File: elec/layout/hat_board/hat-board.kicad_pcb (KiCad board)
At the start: 4 copper layers, 108 x 115.9 mm, 82 parts, among them P1 HatButtonAntenna, U1 _NXP_Semicon_PN5321A3HN_C106_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, U10 _OPSCO_Optoelectronics_SK6805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, U11 _OPSCO_Optoelectronics_SK6805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, U12 _OPSCO_Optoelectronics_SK6805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, U13 _OPSCO_Optoelectronics_SK6805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, U14 _OPSCO_Optoelectronics_SK6805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, U15 _OPSCO_Optoelectronics_SK6805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, U16 _OPSCO_Optoelectronics_SK6805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, U17 _OPSCO_Optoelectronics_SK6805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, U18 _OPSCO_Optoelectronics_SK6805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, U19 _OPSCO_Optoelectronics_SK6805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, U2 _OPSCO_Optoelectronics_SK6805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, U20 _OPSCO_Optoelectronics_SK6805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, U21 _OPSCO_Optoelectronics_SK6805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, U22 _OPSCO_Optoelectronics_SK6805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, U23 _OPSCO_Optoelectronics_SK6805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, U24 _OPSCO_Optoelectronics_SK6805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, U25 _Microchip_Tech_CAP1188_1_CP_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, U3 _OPSCO_Optoelectronics_SK6805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, U4 _OPSCO_Optoelectronics_SK6805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, U5 _OPSCO_Optoelectronics_SK6805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, U6 _OPSCO_Optoelectronics_SK6805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, U7 _OPSCO_Optoelectronics_SK6805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, U8 _OPSCO_Optoelectronics_SK6805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, U9 _OPSCO_Optoelectronics_SK6805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

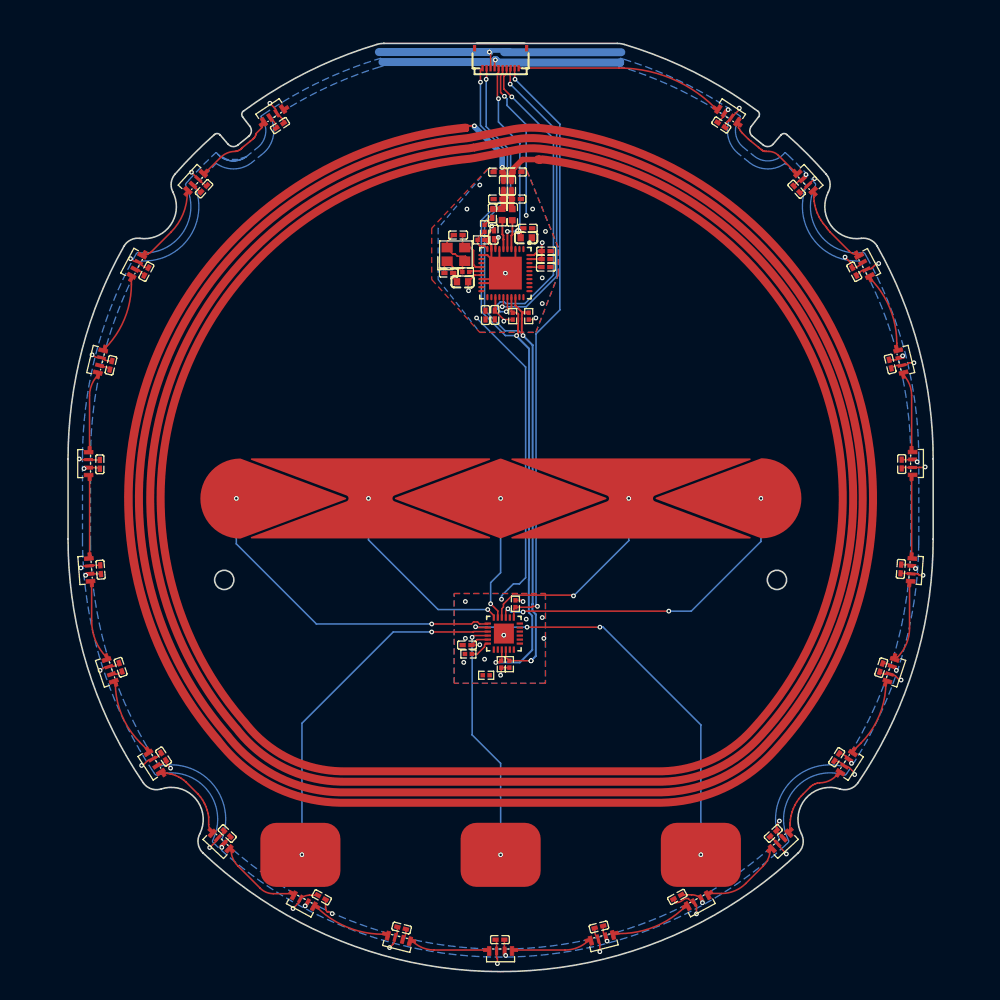
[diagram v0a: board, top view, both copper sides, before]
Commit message: Fix: hat layout
Depends on #23
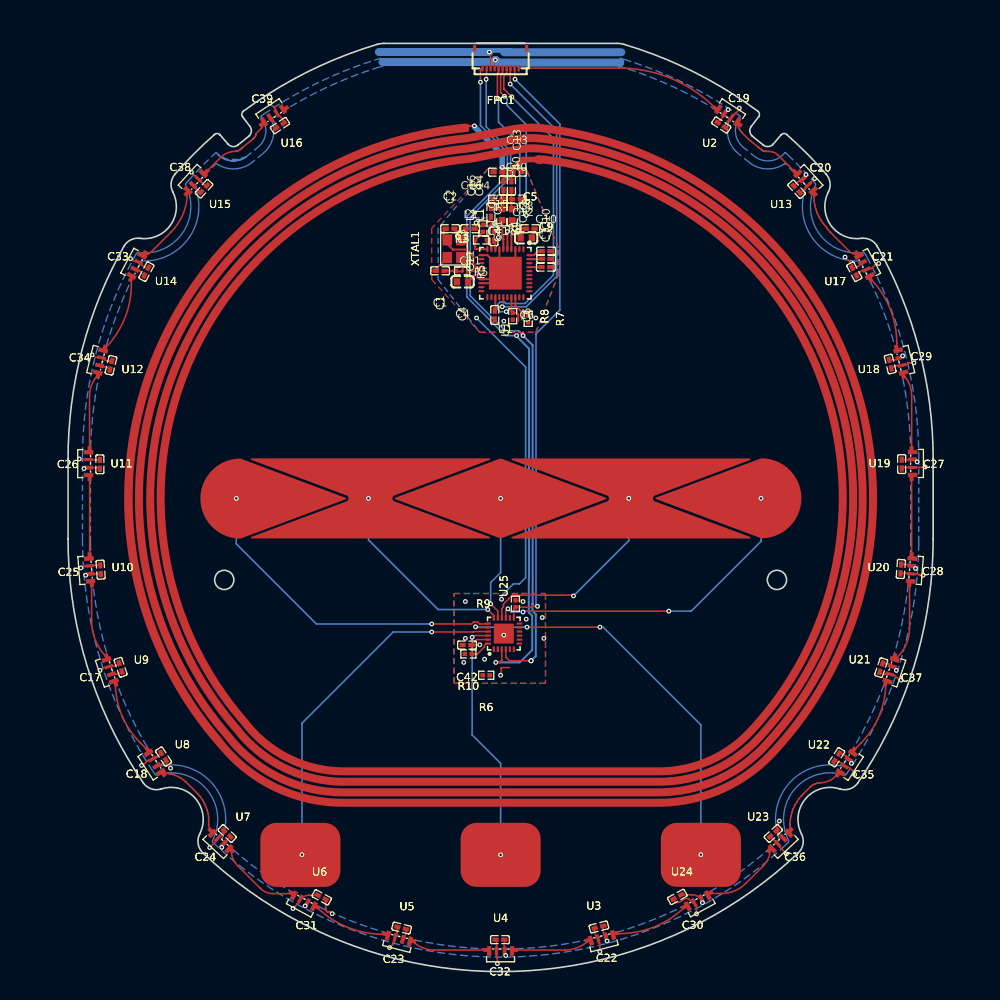
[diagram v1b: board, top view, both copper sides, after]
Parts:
- removed R1, R2: 5.1kΩ ±1% 62.5mW, lcsc:R0402
- C1, C10, C11, C12, C13, C14, C15, C16, C17, C18, C19, C2, C20, C21, C22, C23, C24, C25, C26, C27, C28, C29, C3, C30, C31, C32, C33, C34, C35, C36, C37, C38, C39, C40, C41, C42, C5, C6, C7, C9: footprint lcsc:C0402 -> atopile:C0402-b3ef17
- C4, C8: footprint lcsc:C0603 -> atopile:C0603-bd72f6
- FPC1: value TE_Connectivity_1_2328702_0 -> (none); footprint lcsc:FPC-SMD_10P-P0.50_HDGC_0.5K-HX-10PWB -> atopile:FPC-SMD_10P-P0.50_HDGC_0.5K-HX-10PWB-40cf1c
- L1, L2: value 560nH ±5% 450mA 480mΩ -> (none); footprint lcsc:IND-SMD_L1.6-W0.8-1 -> atopile:IND-SMD_L1.6-W0.8-1-cea827
- P1: value HatButtonAntenna -> (none)
- R10, R3, R4, R5, R6, R9: footprint lcsc:R0402 -> atopile:R0402-56259e
- R7, R8: value 5.1kΩ ±1% 62.5mW -> 100kΩ ±1% 62.5mW; footprint lcsc:R0402 -> atopile:R0402-56259e
- U1: value _NXP_Semicon_PN5321A3HN_C106_51 -> (none); footprint lcsc:QFN-40_L6.0-W6.0-P0.50-BL-EP4.1 -> atopile:QFN-40_L6.0-W6.0-P0.50-BL-EP4.1-54a13c
- U10, U11, U12, U13, U14, U15, U16, U17, U18, U19, U2, U20, U21, U22, U23, U24, U3, U4, U5, U6, U7, U8, U9: value _OPSCO_Optoelectronics_SK6805SIDE_G_001 -> (none); footprint lcsc:LED-SMD_4P-L3.5-W1.6_SK6805SIDE-G-001 -> atopile:LED-SMD_4P-L3.5-W1.6_SK6805SIDE-G-001-1abe24
- U25: value _Microchip_Tech_CAP1188_1_CP_TR -> (none); footprint lcsc:QFN-24_L4.0-W4.0-P0.50-TL-EP2.5 -> atopile:QFN-24_L4.0-W4.0-P0.50-BL-EP2.5-58dc27
- XTAL1: value Crystal -> (none); footprint lcsc:CRYSTAL-SMD_4P-L3.2-W2.5-BL -> atopile:CRYSTAL-SMD_4P-L3.2-W2.5-BL-e199c8
- moved R8 43.5 mm to (153.3, 68.4)
- moved R7 43.2 mm to (155.2, 68.7)
- moved C11 11.0 mm to (148.0, 57.5), turned to 180 degrees
- moved C9 4.45 mm to (157.5, 61.2)
- moved C5 4.28 mm to (155.5, 57.5)
- moved C2 1.28 mm to (145.5, 57.5), turned to 0 degrees
- moved C1 1.13 mm to (144.2, 62.7), turned to 180 degrees
- moved XTAL1 0.74 mm to (146.0, 60.0), turned to 90 degrees
- moved R3 0.49 mm to (147.0, 62.7)
- moved C12 0.23 mm to (150.6, 55.4)
- moved R4 0.20 mm to (149.6, 57.4)
- moved C3 0.20 mm to (151.0, 58.4)
- turned U25 to 0 degrees
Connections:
- net aux1 renamed AUX1
- net aux2 renamed AUX2
- net capacitive_sensor-net renamed RESET
- net dout renamed leds[22]-DOUT
- net led1 renamed LED1
- net led2 renamed LED2
- net led3 renamed LED3
- net led4 renamed LED4
- net led5 renamed LED5
- net led6 renamed LED6
- net led7 renamed LED7
- net led8 renamed LED8
- net loadmod renamed LOADMOD
- net miso_p71 renamed MISO_P71
- net nfc-net-1 renamed RX
- net nfc-net-2 renamed TX1
- net nfc-net-3 renamed OSCIN
- net nfc-net-4 renamed SVDD
- net nfc-net-5 renamed TX2
- net nfc-net-6 renamed OSCOUT
- net p30_uart_rx renamed P30_UART_RX
- net p31_uart_tx renamed P31_UART_TX
- net p32_int0 renamed P32_INT0
- net p33_int1 renamed P33_INT1
- net p34_sic_clk renamed P34_SIC_CLK
- net rstpd_n renamed RSTPD_N
- net sck_p72 renamed SCK_P72
- net sigin renamed SIGIN
- net signal renamed DIN
- net signal-1 renamed DOUT-5
- net signal-10 renamed DOUT-6
- net signal-11 renamed DIN-2
- net signal-12 renamed DIN-5
- net signal-13 renamed DIN-3
- net signal-14 renamed DOUT-3
- net signal-15 renamed DOUT-7
- net signal-16 renamed DIN-6
- net signal-17 renamed DOUT-8
- net signal-18 renamed DOUT-4
- net signal-19 renamed DIN-4
- net signal-2 renamed DOUT-2
- net signal-20 renamed DIN-1
- net signal-21 renamed DOUT-9
- net signal-3 renamed DIN-8
- net signal-4 renamed DOUT-10
- net signal-5 renamed DIN-7
- net signal-6 renamed DOUT
- net signal-7 renamed DOUT-11
- net signal-8 renamed DIN-9
- net signal-9 renamed DOUT-1
- net sigout renamed SIGOUT
- net spi_csh renamed SPI_CSh
- net wake_spi_mosi renamed WAKE_SPI_MOSI
- C11 pad 1: gnd -> VMID
- C11 pad 2: lv -> gnd
- R5 pad 1: gnd -> VMID
- R6 pad 1: capacitive_sensor.address-signal -> ADDR_COMM
- U1 pad 19: p35 -> nfc.nfc_ic-net
- U1 pad 20: nfc.nfc_ic-net -> nfc.nfc_ic.footprint.pins[12].net-net
- U1 pad 21: nfc.nfc_ic-net -> nfc.nfc_ic.footprint.pins[13].net-net
- U1 pad 22: nfc.nfc_ic-net -> nfc.nfc_ic.footprint.pins[14].net-net
- U1 pad 9: gnd -> VMID
- U25 pad 14: addr_comm -> ADDR_COMM
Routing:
- net power_3v3: track 86.4 -> 77.7 mm, vias 12 -> 6
- net gnd: track 196.0 -> 188.3 mm, vias 43 -> 35
- net VMID: track 0.00 -> 7.41 mm, vias 0 -> 2
- net OSCIN: track 5.80 -> 8.31 mm
- net (no net): track 0.00 -> 2.00 mm, vias 0 -> 4
- net nfc.oscillator-net: track 6.65 -> 4.67 mm
- net reset: track 40.7 -> 39.2 mm
- net i2c_scl: track 91.7 -> 91.0 mm
- net RX: track 3.37 -> 4.11 mm
- added copper zone on B.Cu, net (none)
- added copper zone on In1.Cu, net (none)
- removed copper zone on B.Cu, net lv

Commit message: layout complete, some drcs to resolve
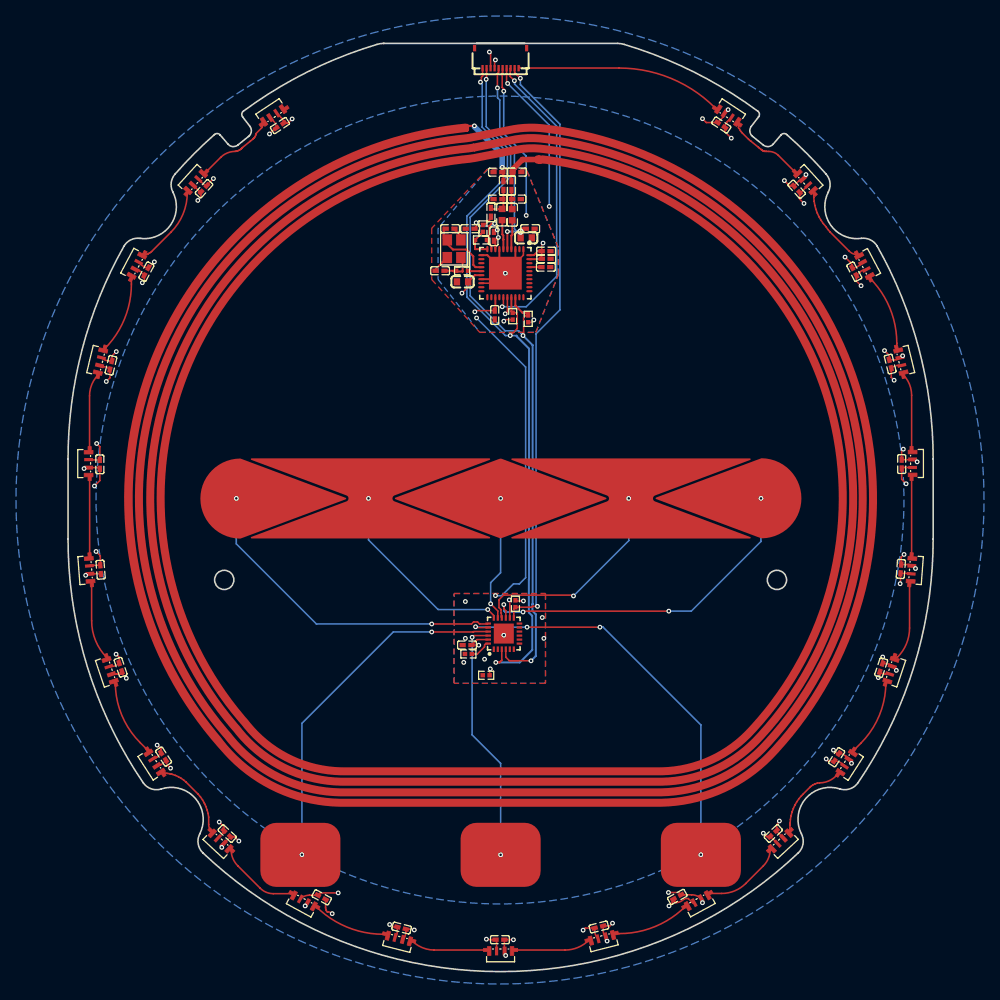
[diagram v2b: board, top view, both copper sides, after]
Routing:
- net gnd: track 188.3 -> 156.6 mm, vias 35 -> 37
- net ADDR_COMM: track 0.00 -> 13.1 mm, vias 0 -> 2
- net power_3v3: track 77.7 -> 85.2 mm, vias 6 -> 11
- net power_5v: track 77.7 -> 73.2 mm, vias 19 -> 37
- net i2c_sda: track 91.5 -> 93.6 mm
- net i2c_scl: track 91.0 -> 93.0 mm, vias 4 -> 3
- net (no net): track 2.00 -> 0.00 mm, vias 4 -> 0
- net reset: track 39.2 -> 37.3 mm, vias 2 -> 3
- net slider_4: track 42.1 -> 43.7 mm
- net slider_3: track 26.0 -> 27.0 mm
- added copper zone on B.Cu, net gnd
- added copper zone on In1.Cu, net power_5v
- removed copper zone on B.Cu, net (none)
- removed copper zone on In1.Cu, net (none)
- removed copper zone on B.Cu, net power_5v

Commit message: resolve DRCs + cleanup
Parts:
- moved C1 0.61 mm to (144.9, 62.7)
- moved C3 0.31 mm to (151.3, 58.4)
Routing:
- net gnd: track 156.6 -> 161.1 mm, vias 37 -> 40
- net nfc.oscillator-net: track 4.46 -> 3.52 mm
- net i2c_scl: track 93.0 -> 92.4 mm
- net OSCOUT: track 1.49 -> 2.02 mm
